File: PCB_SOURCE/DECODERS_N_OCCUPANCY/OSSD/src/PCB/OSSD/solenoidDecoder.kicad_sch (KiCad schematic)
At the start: 6 parts, among them J62 Screw_Terminal_01x04

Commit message: changed BOM and CPL for OSSD due to stock amount issues for screw ternminals
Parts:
- J62: JLCPCB Part# C395831 -> C880574
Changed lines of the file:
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@@
 			)
 		)
-		(property "JLCPCB Part#" "C395831"
+		(property "JLCPCB Part#" "C880574"
 			(at 39.37 72.39 0)
 			(effects

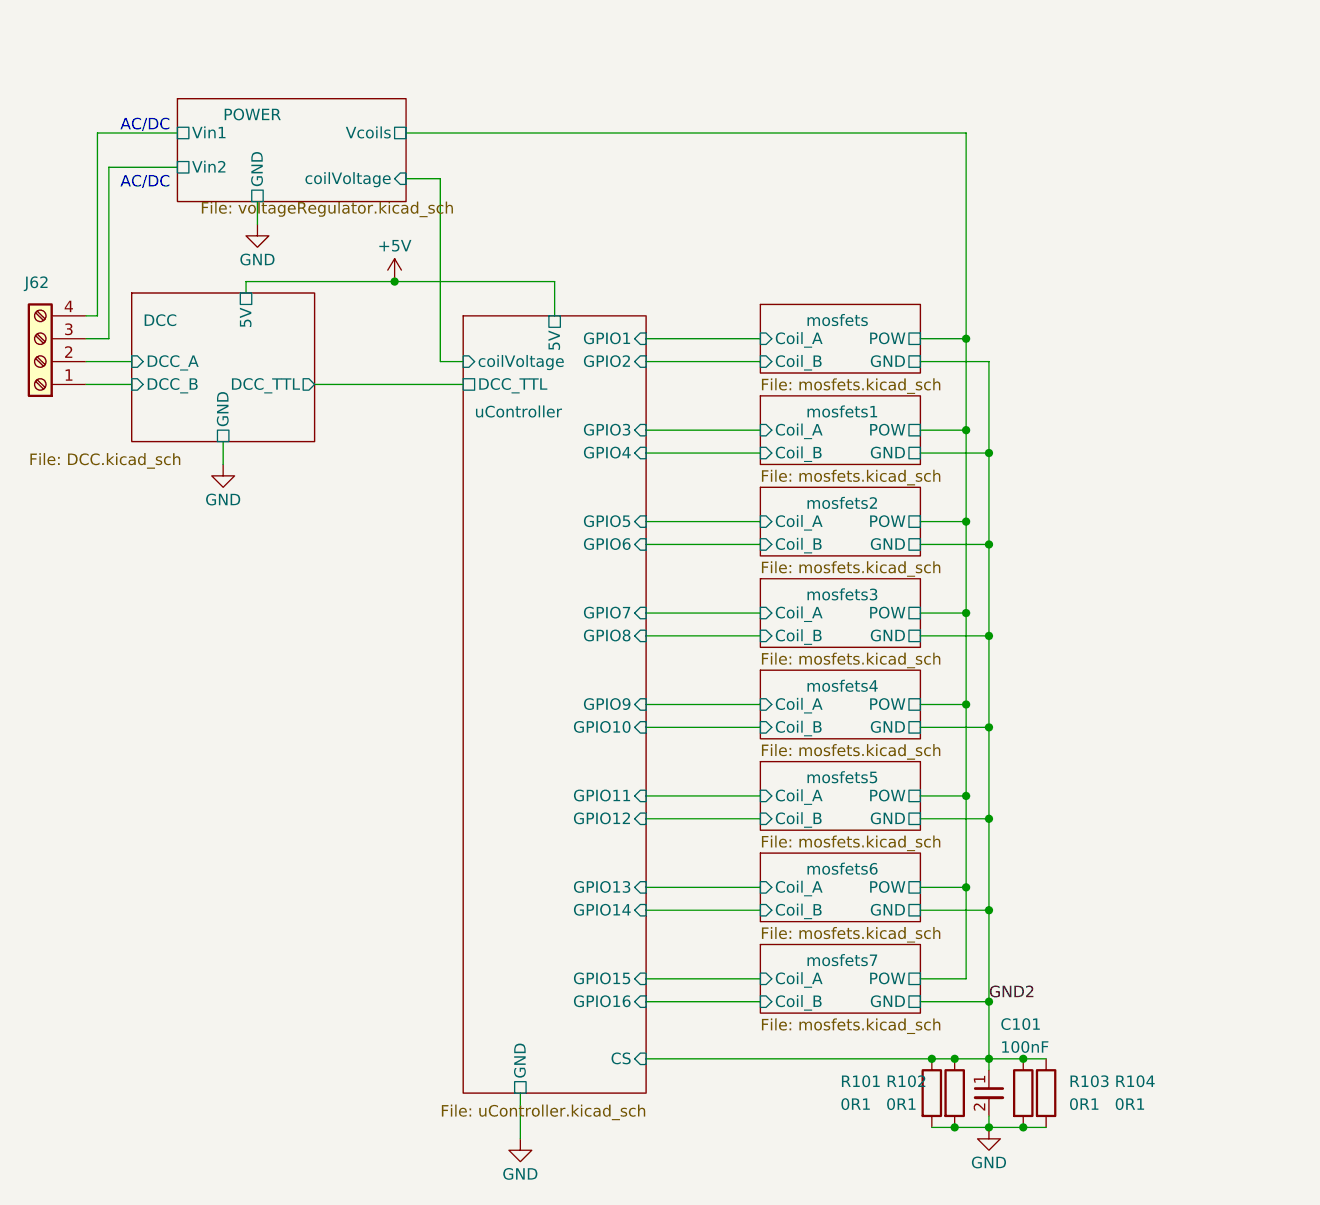
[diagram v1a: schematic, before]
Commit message: added S88 current sense to releases and update OSSD decoder
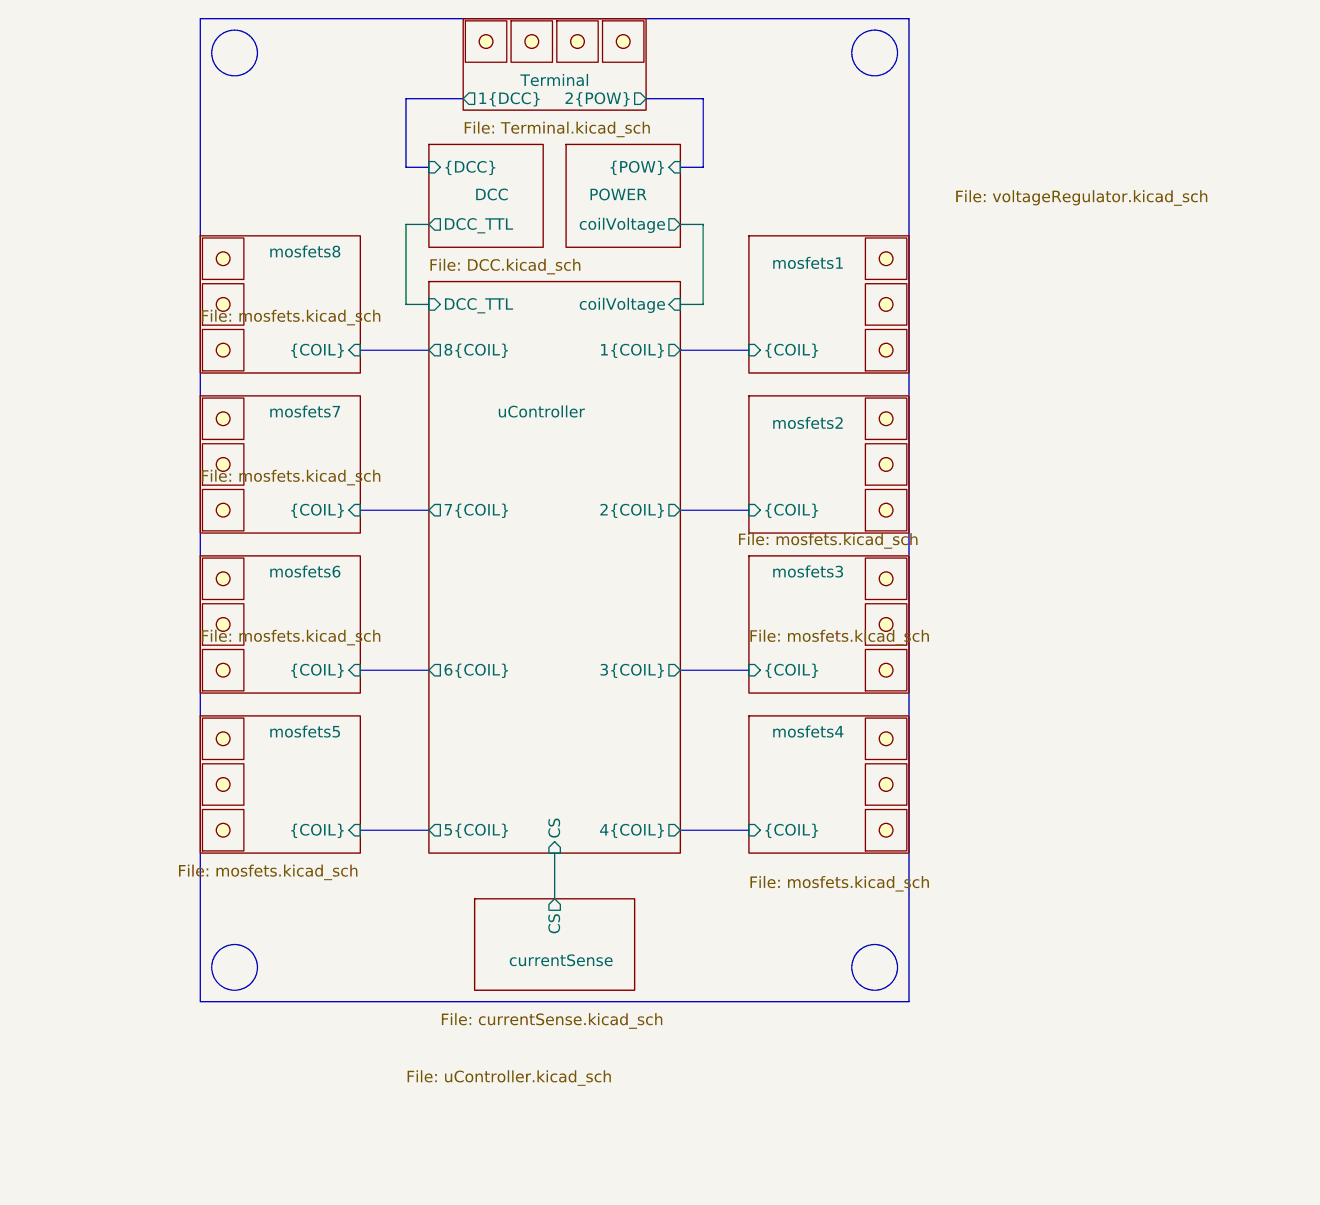
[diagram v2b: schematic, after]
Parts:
- removed C101: 100nF, Capacitor_SMD:C_0402_1005Metric, symbol capacitor_miscellaneous:C_0402_100nF
- removed J62: Screw_Terminal_01x04, Connector_Phoenix_MC:PhoenixContact_MC_1,5_4-G-3.5_1x04_P3.50mm_Horizontal, symbol Connector:Screw_Terminal_01x04
- removed R101, R102, R103, R104: 0R1, Resistor_SMD:R_1206_3216Metric, symbol resistors_1206:R_0R1_1206
- added u101, u102, u103, u104, u105, u106, u107, u108, u109, u110, u111, u112, u113, u114, u115, u116, u117, u118, u119, u120, u121, u122, u123, u124, u125, u126, u127, u128: ~, symbol custom_kicad_lib_sk:screwterminal
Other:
- removed sheet mosfets
- added sheet Terminal (Terminal.kicad_sch)
- added sheet currentSense (currentSense.kicad_sch)
- added sheet mosfets8 (mosfets.kicad_sch)
- sheet DCC ports: added {DCC}; removed 5V, DCC_A, DCC_B, GND
- sheet POWER ports: added {POW}; removed GND, Vcoils, Vin1, Vin2
- sheet mosfets1 ports: added {COIL}; removed Coil_A, Coil_B, GND, POW
- sheet mosfets2 ports: added {COIL}; removed Coil_A, Coil_B, GND, POW
- sheet mosfets3 ports: added {COIL}; removed Coil_A, Coil_B, GND, POW
- sheet mosfets4 ports: added {COIL}; removed Coil_A, Coil_B, GND, POW
- sheet mosfets5 ports: added {COIL}; removed Coil_A, Coil_B, GND, POW
- sheet mosfets6 ports: added {COIL}; removed Coil_A, Coil_B, GND, POW
- sheet mosfets7 ports: added {COIL}; removed Coil_A, Coil_B, GND, POW
- sheet uController ports: added 1{COIL}, 2{COIL}, 3{COIL}, 4{COIL}, 5{COIL}, 6{COIL}, 7{COIL}, 8{COIL}; removed 5V, GND, GPIO1, GPIO10, GPIO11, GPIO12, GPIO13, GPIO14, GPIO15, GPIO16, GPIO2, GPIO3, GPIO4, GPIO5, GPIO6, GPIO7, GPIO8, GPIO9
- note removed: "AC/DC"
